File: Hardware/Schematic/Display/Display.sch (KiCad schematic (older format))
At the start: 18 parts, among them J1 Conn_01x32, J10 Conn_01x02, J8 Conn_01x24, Q1 Q_PJFET_GSD

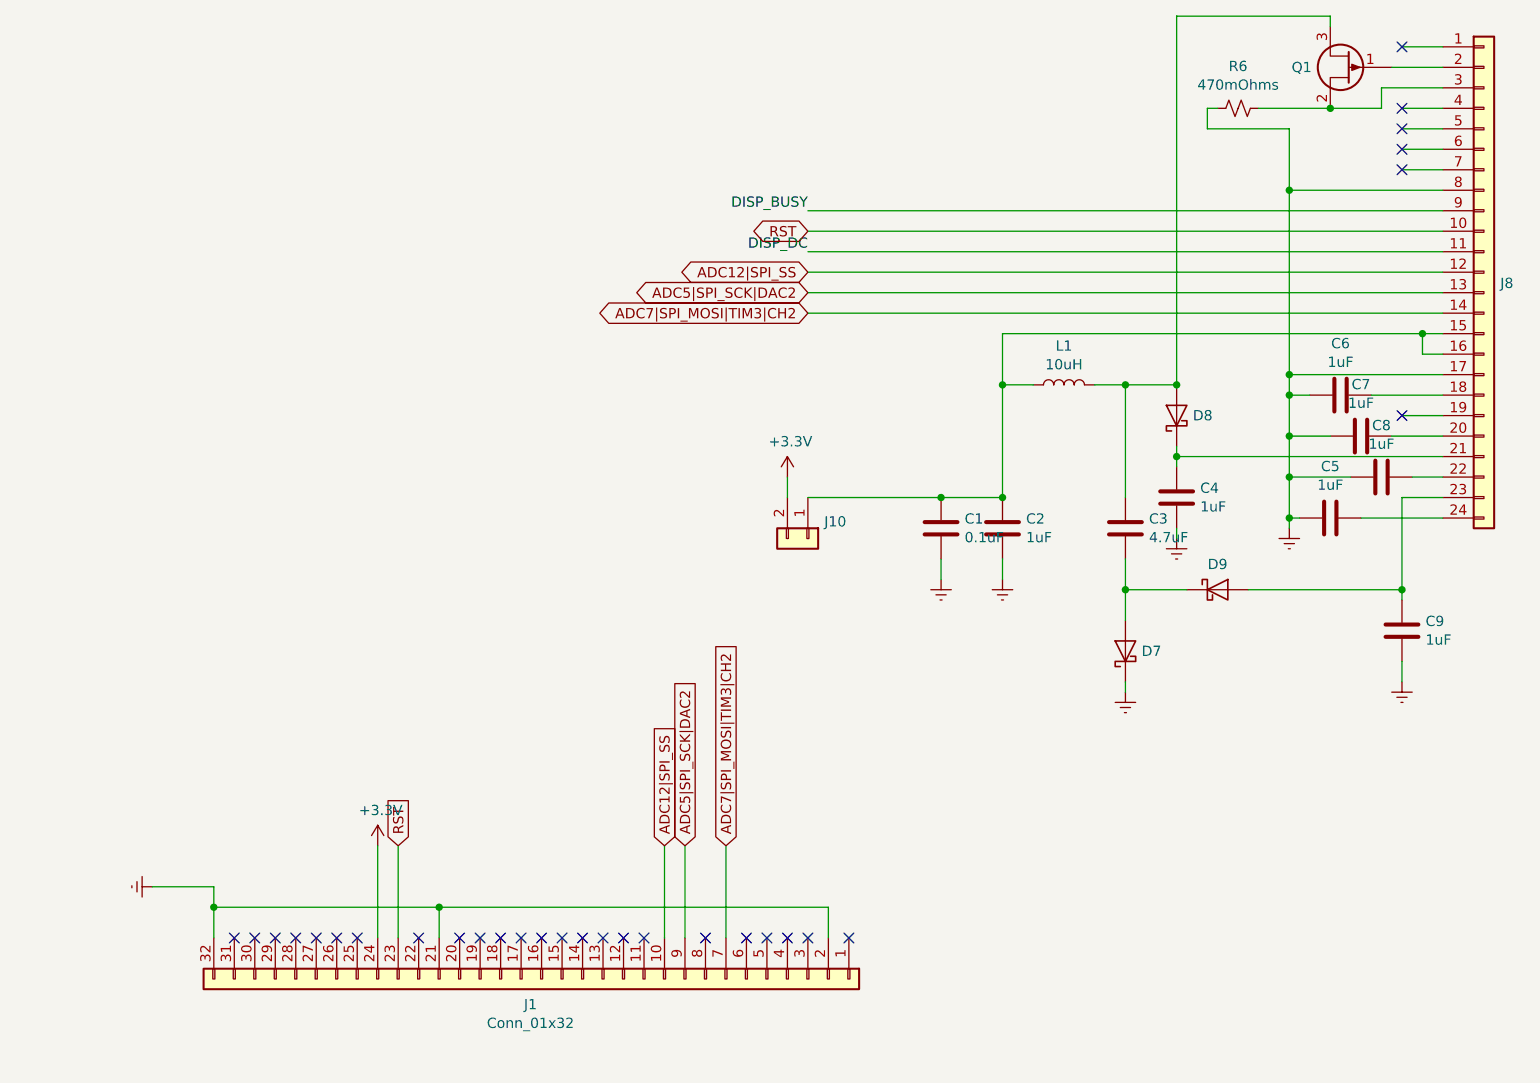
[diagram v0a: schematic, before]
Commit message: Added male 02x16 header to auxillary boards so they can be "stacked" together
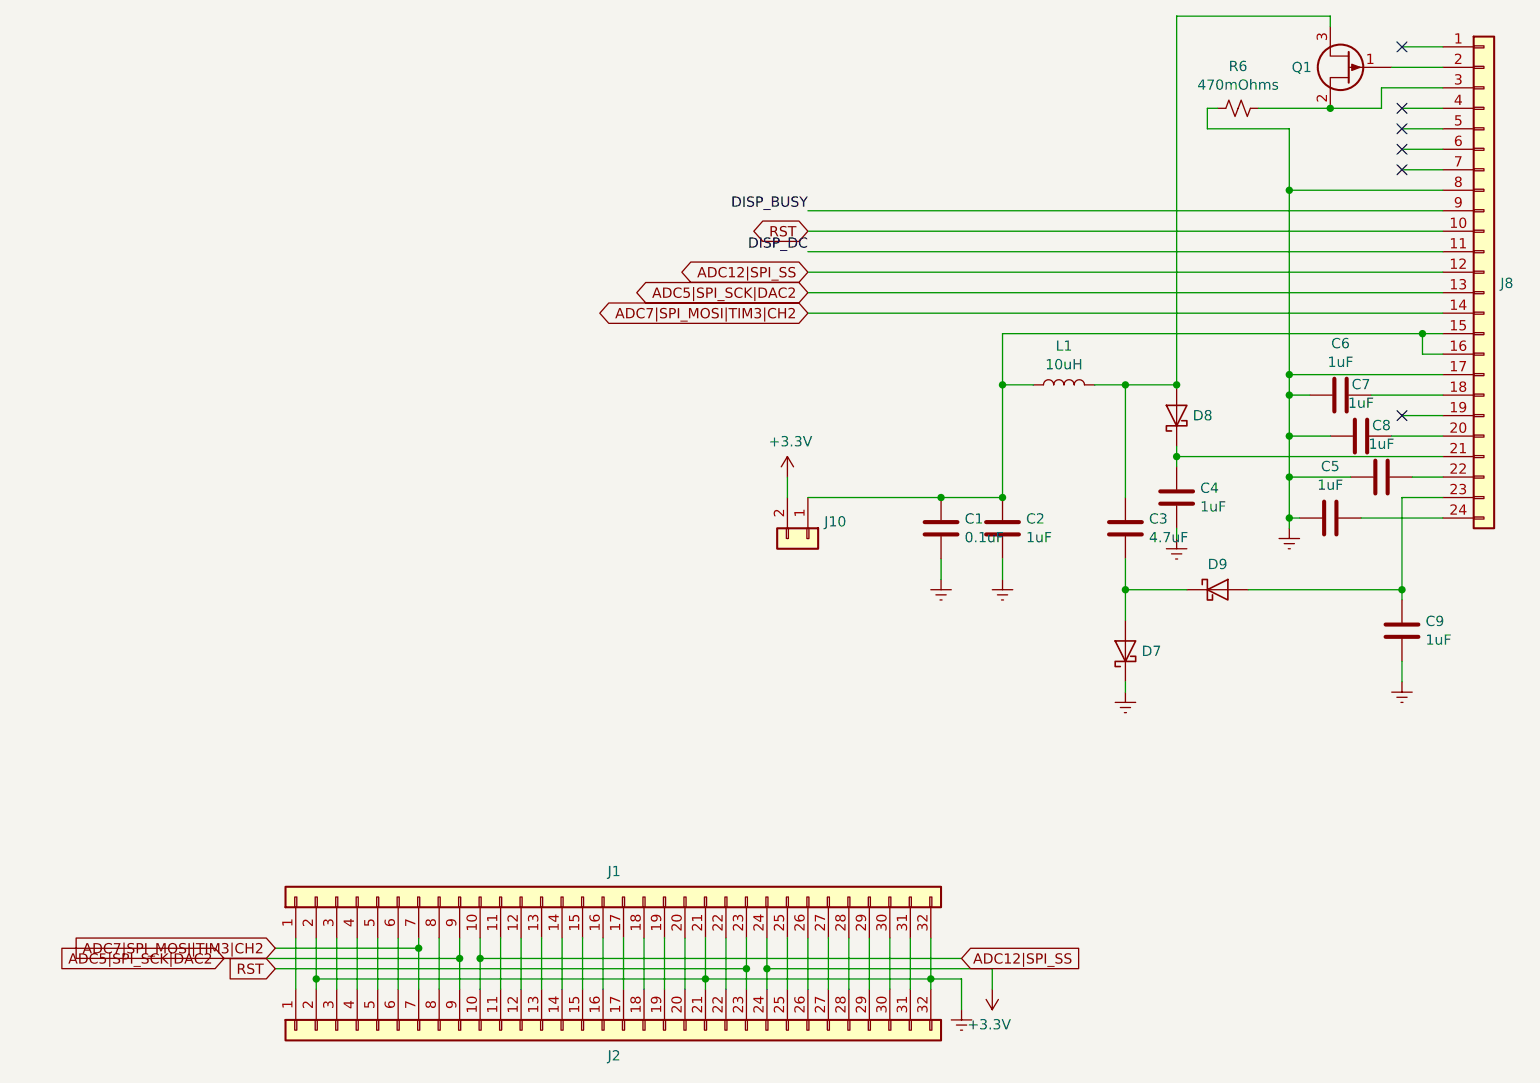
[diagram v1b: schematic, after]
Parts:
- added J2: Conn_01x32, Connector_PinSocket_2.54mm:PinSocket_2x16_P2.54mm_Horizontal, symbol Connector_Generic:Conn_01x32
- J1: footprint Connector_PinSocket_2.54mm:PinSocket_2x16_P2.54mm_Horizontal -> Connector_PinHeader_2.54mm:PinHeader_2x16_P2.54mm_Horizontal
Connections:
- net +3V3: now also J2.24 (Pin_24)
- net ADC12|SPI_SS: now also J2.10 (Pin_10)
- net ADC5|SPI_SCK|DAC2: now also J2.9 (Pin_9)
- net ADC7|SPI_MOSI|TIM3|CH2: now also J2.7 (Pin_7)
- net Earth: now also J2.2 (Pin_2), J2.21 (Pin_21), J2.32 (Pin_32)
- net RST: now also J2.23 (Pin_23)
- net at J1.1 (Pin_1): now also J2.1 (Pin_1)
- net at J1.11 (Pin_11): now also J2.11 (Pin_11)
- net at J1.12 (Pin_12): now also J2.12 (Pin_12)
- net at J1.13 (Pin_13): now also J2.13 (Pin_13)
- net at J1.14 (Pin_14): now also J2.14 (Pin_14)
- net at J1.15 (Pin_15): now also J2.15 (Pin_15)
- net at J1.16 (Pin_16): now also J2.16 (Pin_16)
- net at J1.17 (Pin_17): now also J2.17 (Pin_17)
- net at J1.18 (Pin_18): now also J2.18 (Pin_18)
- net at J1.19 (Pin_19): now also J2.19 (Pin_19)
- net at J1.20 (Pin_20): now also J2.20 (Pin_20)
- net at J1.22 (Pin_22): now also J2.22 (Pin_22)
- net at J1.25 (Pin_25): now also J2.25 (Pin_25)
- net at J1.26 (Pin_26): now also J2.26 (Pin_26)
- net at J1.27 (Pin_27): now also J2.27 (Pin_27)
- net at J1.28 (Pin_28): now also J2.28 (Pin_28)
- net at J1.29 (Pin_29): now also J2.29 (Pin_29)
- net at J1.3 (Pin_3): now also J2.3 (Pin_3)
- net at J1.30 (Pin_30): now also J2.30 (Pin_30)
- net at J1.31 (Pin_31): now also J2.31 (Pin_31)
- net at J1.4 (Pin_4): now also J2.4 (Pin_4)
- net at J1.5 (Pin_5): now also J2.5 (Pin_5)
- net at J1.6 (Pin_6): now also J2.6 (Pin_6)
- net at J1.8 (Pin_8): now also J2.8 (Pin_8)
- no-connect marks 30 -> 6
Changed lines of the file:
@@
 EESchema Schematic File Version 4
+LIBS:Display-cache
 EELAYER 29 0
 EELAYER END
@@
 $Comp
 L Connector_Generic:Conn_01x32 J1
-U 1 1 5D06E94D
-P 3500 7000
-F 0 "J1" V 3625 6946 50  0000 C CNN
-F 1 "Conn_01x32" V 3716 6946 50  0000 C CNN
-F 2 "Connector_PinSocket_2.54mm:PinSocket_2x16_P2.54mm_Horizontal" H 3500 7000 50  0001 C CNN
-F 3 "~" H 3500 7000 50  0001 C CNN
-	1    3500 7000
-	0    1    1    0
-$EndComp
+U 1 1 5D07BB73
+P 3800 6600
+F 0 "J1" V 3925 6546 50  0000 C CNN
+F 1 "Conn_01x32" V 4016 6546 50  0001 C CNN
+F 2 "Connector_PinHeader_2.54mm:PinHeader_2x16_P2.54mm_Horizontal" H 3800 6600 50  0001 C CNN
+F 3 "~" H 3800 6600 50  0001 C CNN
+	1    3800 6600
+	0    -1   -1   0
+$EndComp
+$Comp
+L Connector_Generic:Conn_01x32 J2
+U 1 1 5D083701
+P 3800 7250
+F 0 "J2" V 3925 7196 50  0000 C CNN
+F 1 "Conn_01x32" V 4016 7196 50  0001 C CNN
+F 2 "Connector_PinSocket_2.54mm:PinSocket_2x16_P2.54mm_Horizontal" H 3800 7250 50  0001 C CNN
+F 3 "~" H 3800 7250 50  0001 C CNN
+	1    3800 7250
+	0    -1   1    0
+$EndComp
+Wire Wire Line
+	5400 7050 5400 7000
+Wire Wire Line
+	5300 6800 5300 7050
+Wire Wire Line
+	5200 7050 5200 6800
+Wire Wire Line
+	5100 6800 5100 7050
+Wire Wire Line
+	5000 7050 5000 6800
+Wire Wire Line
+	4900 7050 4900 6800
+Wire Wire Line
+	4800 7050 4800 6800
+Wire Wire Line
+	4700 7050 4700 6800
+Wire Wire Line
+	4600 7050 4600 6950
+Wire Wire Line
+	4500 6800 4500 6950
+Wire Wire Line
+	4400 7050 4400 6800
+Wire Wire Line
+	4300 6800 4300 7000
+Wire Wire Line
+	4200 7050 4200 6800
+Wire Wire Line
+	4100 6800 4100 7050
+Wire Wire Line
+	4000 7050 4000 6800
+Wire Wire Line
+	3900 6800 3900 7050
+Wire Wire Line
+	3800 7050 3800 6800
+Wire Wire Line
+	3700 6800 3700 7050
+Wire Wire Line
+	3600 7050 3600 6800
+Wire Wire Line
+	3500 6800 3500 7050
+Wire Wire Line
+	3400 7050 3400 6800
+Wire Wire Line
+	3300 6800 3300 7050
+Wire Wire Line
+	3200 7050 3200 6900
+Wire Wire Line
+	3100 6800 3100 6900
+Wire Wire Line
+	3000 7050 3000 6800
+Wire Wire Line
+	2900 6800 2900 6850
+Wire Wire Line
+	2800 6800 2800 7050
+Wire Wire Line
+	2700 7050 2700 6800
+Wire Wire Line
+	2600 6800 2600 7050
+Wire Wire Line
+	2500 7050 2500 6800
+Wire Wire Line
+	2400 6800 2400 7000
+Wire Wire Line
+	2300 7050 2300 6800
+Wire Wire Line
+	5400 7000 5550 7000
+Wire Wire Line
+	5550 7000 5550 7150
+Connection ~ 5400 7000
+Wire Wire Line
+	5400 7000 5400 6800
+Wire Wire Line
+	4300 7000 5400 7000
+Connection ~ 4300 7000
+Wire Wire Line
+	4300 7000 4300 7050
+Wire Wire Line
+	2400 7000 4300 7000
+Connection ~ 2400 7000
+Wire Wire Line
+	2400 7000 2400 7050
 $Comp
 L power:Earth #PWR0101
-U 1 1 5D074B64
-P 1600 6550
-F 0 "#PWR0101" H 1600 6300 50  0001 C CNN
-F 1 "Earth" H 1600 6400 50  0001 C CNN
-F 2 "" H 1600 6550 50  0001 C CNN
-F 3 "~" H 1600 6550 50  0001 C CNN
-	1    1600 6550
-	0    1    1    0
-$EndComp
-Wire Wire Line
-	1900 6800 1900 6650
-Wire Wire Line
-	1900 6550 1600 6550
-Wire Wire Line
-	1900 6650 3000 6650
-Wire Wire Line
-	3000 6650 3000 6800
-Connection ~ 1900 6650
-Wire Wire Line
-	1900 6650 1900 6550
-Wire Wire Line
-	3000 6650 4900 6650
-Wire Wire Line
-	4900 6650 4900 6800
-Connection ~ 3000 6650
+U 1 1 5D10E6AE
+P 5550 7150
+F 0 "#PWR0101" H 5550 6900 50  0001 C CNN
+F 1 "Earth" H 5550 7000 50  0001 C CNN
+F 2 "" H 5550 7150 50  0001 C CNN
+F 3 "~" H 5550 7150 50  0001 C CNN
+	1    5550 7150
+	1    0    0    -1
+$EndComp
 $Comp
 L power:+3.3V #PWR0102
-U 1 1 5D08108E
-P 2700 6350
-F 0 "#PWR0102" H 2700 6200 50  0001 C CNN
-F 1 "+3.3V" H 2715 6523 50  0000 C CNN
-F 2 "" H 2700 6350 50  0001 C CNN
-F 3 "" H 2700 6350 50  0001 C CNN
-	1    2700 6350
-	1    0    0    -1
-$EndComp
-Wire Wire Line
-	2700 6800 2700 6350
-Wire Wire Line
-	2800 6800 2800 6350
-Wire Wire Line
-	4100 6800 4100 6350
-Wire Wire Line
-	4200 6800 4200 6350
-Wire Wire Line
-	4400 6800 4400 6350
-Text GLabel 2800 6350 1    50   Input ~ 0
+U 1 1 5D10F70A
+P 5700 7050
+F 0 "#PWR0102" H 5700 6900 50  0001 C CNN
+F 1 "+3.3V" H 5715 7223 50  0000 C CNN
+F 2 "" H 5700 7050 50  0001 C CNN
+F 3 "" H 5700 7050 50  0001 C CNN
+	1    5700 7050
+	-1   0    0    1
+$EndComp
+Wire Wire Line
+	4600 6950 5700 6950
+Wire Wire Line
+	5700 6950 5700 7050
+Connection ~ 4600 6950
+Wire Wire Line
+	4600 6950 4600 6800
+Wire Wire Line
+	4500 6950 2200 6950
+Connection ~ 4500 6950
+Wire Wire Line
+	4500 6950 4500 7050
+Text GLabel 2200 6950 0    50   Input ~ 0
 RST
-Text GLabel 4100 6350 1    50   Input ~ 0
+Wire Wire Line
+	3200 6900 5550 6900
+Connection ~ 3200 6900
+Wire Wire Line
+	3200 6900 3200 6800
+Text GLabel 5550 6900 2    50   Input ~ 0
 ADC12|SPI_SS
-Text GLabel 4200 6350 1    50   Input ~ 0
+Wire Wire Line
+	3100 6900 1950 6900
+Connection ~ 3100 6900
+Wire Wire Line
+	3100 6900 3100 7050
+Text GLabel 1950 6900 0    50   Input ~ 0
 ADC5|SPI_SCK|DAC2
-Text GLabel 4400 6350 1    50   Input ~ 0
+Wire Wire Line
+	2900 6850 2200 6850
+Connection ~ 2900 6850
+Wire Wire Line
+	2900 6850 2900 7050
+Text GLabel 2200 6850 0    50   Input ~ 0
 ADC7|SPI_MOSI|TIM3|CH2
-NoConn ~ 2000 6800
-NoConn ~ 2100 6800
-NoConn ~ 2200 6800
-NoConn ~ 2300 6800
-NoConn ~ 2400 6800
-NoConn ~ 2500 6800
-NoConn ~ 2600 6800
-NoConn ~ 2900 6800
-NoConn ~ 3100 6800
-NoConn ~ 3200 6800
-NoConn ~ 3300 6800
-NoConn ~ 3400 6800
-NoConn ~ 3500 6800
-NoConn ~ 3600 6800
-NoConn ~ 3700 6800
-NoConn ~ 3800 6800
-NoConn ~ 3900 6800
-NoConn ~ 4000 6800
-NoConn ~ 4300 6800
-NoConn ~ 4500 6800
-NoConn ~ 4600 6800
-NoConn ~ 4700 6800
-NoConn ~ 4800 6800
-NoConn ~ 5000 6800
 $EndSCHEMATC
